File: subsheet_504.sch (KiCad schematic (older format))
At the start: 34 parts, among them J502 Phono LEFT, J503 Phono RIGHT, U504 LF347N_mu, U508 LMC1992CCN_PHY

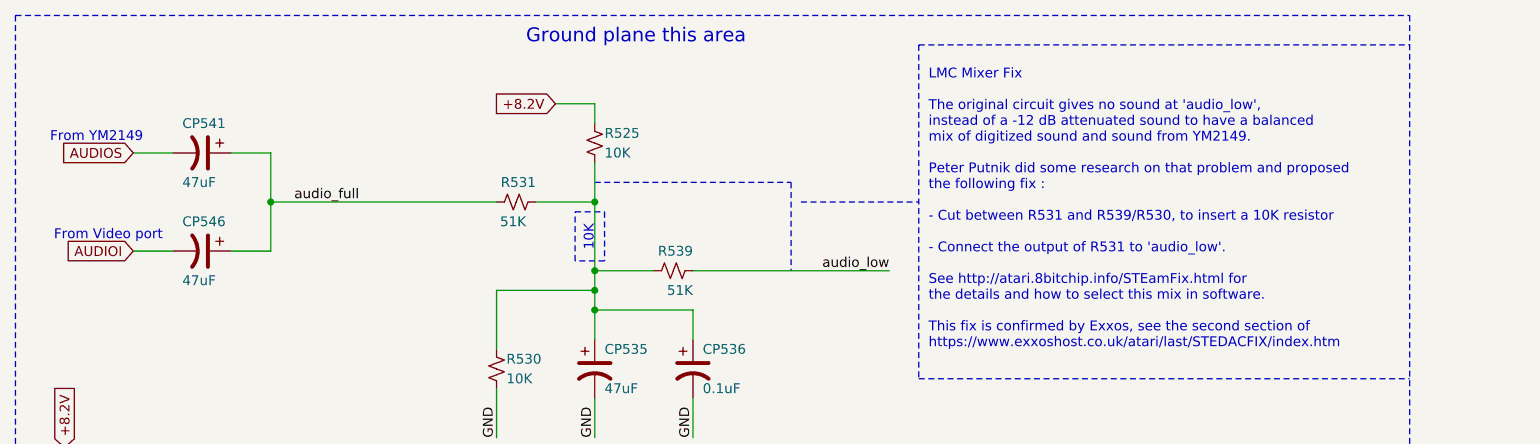
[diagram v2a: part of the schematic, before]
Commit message: Resolves #18 : Apply the LMC mixer fix
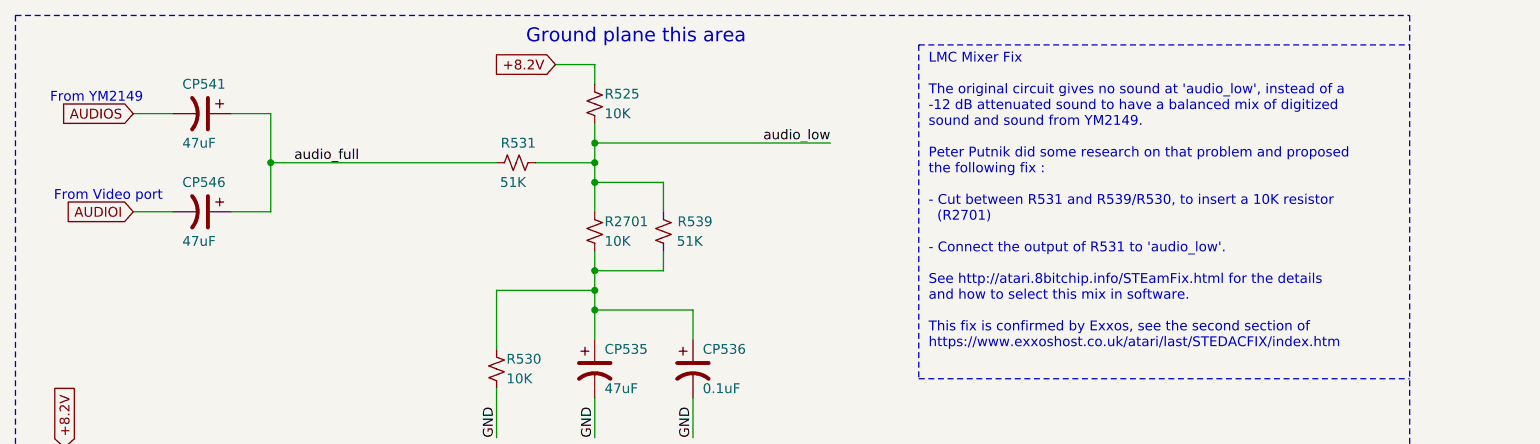
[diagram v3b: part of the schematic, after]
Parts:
- added R2701: 10K, commons_passives_THT:Passive_THT_resistor_W2.54mm_L12.70mm, symbol Device:R_Small_US
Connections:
- net audio_low: now also R525.2, R531.2, R2701.1
- net at CP535.1, CP536.1, R530.1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: now also R2701.2; no longer R525.2, R531.2
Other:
- note added: "LMC Mixer Fix\n\nThe original circuit gives no sound at 'audio_low', instead of a \n-12 dB attenuated sound to have a balanced mix of digitized \nsound and sound from YM2149.\n\nPeter Putnik did some research on that problem and proposed \nthe following fix :\n\n- Cut between R531 and R539/R530, to insert a 10K resistor \n (R2701)\n \n- Connect the output of R531 to 'audio_low'. \n\nSee http://at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"
- note removed: "10K"
- note removed: "LMC Mixer Fix\n\nThe original circuit gives no sound at 'audio_low',\ninstead of a -12 dB attenuated sound to have a balanced\nmix of digitized sound and sound from YM2149.\n\nPeter Putnik did some research on that problem and proposed \nthe following fix :\n\n- Cut between R531 and R539/R530, to insert a 10K resistor\n \n- Connect the output of R531 to 'audio_low'. \n\nSee http://atari.8bitchip.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"
- moved on the sheet: CP541, CP546, R525, R531, R539
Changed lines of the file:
@@
 Text GLabel 1000 3800 0    50   Output ~ 0
 GIL
-Text GLabel 1150 1250 0    50   Input ~ 0
+Text GLabel 1150 1050 0    50   Input ~ 0
 AUDIOS
-Text GLabel 1150 1750 0    50   Input ~ 0
+Text GLabel 1150 1550 0    50   Input ~ 0
 AUDIOI
 NoConn ~ 2900 3600
@@
 L Device:CP1 C?
 U 1 1 60CF0999
-P 1500 1250
+P 1500 1050
 AR Path="/6089D0C2/60CF0999" Ref="C?"  Part="1"
 AR Path="/60B8B7AD/60CF0999" Ref="C?"  Part="1"
@@
 AR Path="/60CC3B10/60CF0999" Ref="C?"  Part="1"
 AR Path="/60CD36E9/60CF0999" Ref="CP541"  Part="1"
-F 0 "CP541" V 1350 1150 50  0000 L CNN
-F 1 "47uF" V 1650 1150 50  0000 L CNN
-F 2 "commons_passives_THT:Passive_THT_capacitor_polarized_W6.35mm_L20.32mm" H 1500 1250 50  0001 C CNN
-F 3 "~" H 1500 1250 50  0001 C CNN
-	1    1500 1250
+F 0 "CP541" V 1350 950 50  0000 L CNN
+F 1 "47uF" V 1650 950 50  0000 L CNN
+F 2 "commons_passives_THT:Passive_THT_capacitor_polarized_W6.35mm_L20.32mm" H 1500 1050 50  0001 C CNN
+F 3 "~" H 1500 1050 50  0001 C CNN
+	1    1500 1050
 	0    1    1    0
 $EndComp
 Wire Wire Line
-	1650 1250 1850 1250
-Wire Wire Line
-	1150 1250 1350 1250
+	1650 1050 1850 1050
+Wire Wire Line
+	1150 1050 1350 1050
 $Comp
 L Device:CP1 C?
 U 1 1 60CF36CC
-P 1500 1750
+P 1500 1550
 AR Path="/6089D0C2/60CF36CC" Ref="C?"  Part="1"
 AR Path="/60B8B7AD/60CF36CC" Ref="C?"  Part="1"
@@
 AR Path="/60CC3B10/60CF36CC" Ref="C?"  Part="1"
 AR Path="/60CD36E9/60CF36CC" Ref="CP546"  Part="1"
-F 0 "CP546" V 1350 1650 50  0000 L CNN
-F 1 "47uF" V 1650 1650 50  0000 L CNN
-F 2 "commons_passives_THT:Passive_THT_capacitor_polarized_W6.35mm_L20.32mm" H 1500 1750 50  0001 C CNN
-F 3 "~" H 1500 1750 50  0001 C CNN
-	1    1500 1750
+F 0 "CP546" V 1350 1450 50  0000 L CNN
+F 1 "47uF" V 1650 1450 50  0000 L CNN
+F 2 "commons_passives_THT:Passive_THT_capacitor_polarized_W6.35mm_L20.32mm" H 1500 1550 50  0001 C CNN
+F 3 "~" H 1500 1550 50  0001 C CNN
+	1    1500 1550
 	0    1    1    0
 $EndComp
 Wire Wire Line
-	1650 1750 1850 1750
-Wire Wire Line
-	1150 1750 1350 1750
+	1650 1550 1850 1550
+Wire Wire Line
+	1150 1550 1350 1550
 $Comp
 L Device:CP1 C?
@@
 L Device:R_Small_US R?
 U 1 1 60CF6F70
-P 3500 1200
+P 3500 1000
 AR Path="/60B3D9E3/60CF6F70" Ref="R?"  Part="1"
 AR Path="/60B8B7AD/60CF6F70" Ref="R?"  Part="1"
@@
 AR Path="/60CC3B10/60CF6F70" Ref="R?"  Part="1"
 AR Path="/60CD36E9/60CF6F70" Ref="R525"  Part="1"
-F 0 "R525" H 3550 1250 50  0000 L CNN
-F 1 "10K" H 3550 1150 50  0000 L CNN
-F 2 "commons_passives_THT:Passive_THT_resistor_W2.54mm_L12.70mm" H 3500 1200 50  0001 C CNN
-F 3 "~" H 3500 1200 50  0001 C CNN
-	1    3500 1200
+F 0 "R525" H 3550 1050 50  0000 L CNN
+F 1 "10K" H 3550 950 50  0000 L CNN
+F 2 "commons_passives_THT:Passive_THT_resistor_W2.54mm_L12.70mm" H 3500 1000 50  0001 C CNN
+F 3 "~" H 3500 1000 50  0001 C CNN
+	1    3500 1000
 	1    0    0    -1
 $EndComp
 Text Label 3000 2700 1    50   ~ 0
 GND
-Text GLabel 3300 1000 0    50   Input ~ 0
+Text GLabel 3300 800  0    50   Input ~ 0
 +8.2V
 Wire Wire Line
@@
 Wire Wire Line
 	3000 2450 3000 2700
-Text Notes 1200 1200 2    50   ~ 0
+Text Notes 1200 1000 2    50   ~ 0
 From YM2149
-Text Notes 1300 1700 2    50   ~ 0
+Text Notes 1300 1500 2    50   ~ 0
 From Video port
-Text Label 2300 1500 2    50   ~ 0
+Text Label 2300 1300 2    50   ~ 0
 audio_full
 $Comp
 L Device:R_Small_US R?
 U 1 1 60D12893
-P 3100 1500
+P 3100 1300
 AR Path="/60B3D9E3/60D12893" Ref="R?"  Part="1"
 AR Path="/60B8B7AD/60D12893" Ref="R?"  Part="1"
@@
 AR Path="/60CC3B10/60D12893" Ref="R?"  Part="1"
 AR Path="/60CD36E9/60D12893" Ref="R531"  Part="1"
-F 0 "R531" V 3200 1400 50  0000 L CNN
-F 1 "51K" V 3000 1450 50  0000 L CNN
-F 2 "commons_passives_THT:Passive_THT_resistor_W2.54mm_L12.70mm" H 3100 1500 50  0001 C CNN
-F 3 "~" H 3100 1500 50  0001 C CNN
-	1    3100 1500
+F 0 "R531" V 3200 1200 50  0000 L CNN
+F 1 "51K" V 3000 1250 50  0000 L CNN
+F 2 "commons_passives_THT:Passive_THT_resistor_W2.54mm_L12.70mm" H 3100 1300 50  0001 C CNN
+F 3 "~" H 3100 1300 50  0001 C CNN
+	1    3100 1300
 	0    -1   -1   0
 $EndComp
@@
 L Device:R_Small_US R?
 U 1 1 60D13044
-P 3900 1850
+P 3850 1650
 AR Path="/60B3D9E3/60D13044" Ref="R?"  Part="1"
 AR Path="/60B8B7AD/60D13044" Ref="R?"  Part="1"
@@
 AR Path="/60CC3B10/60D13044" Ref="R?"  Part="1"
 AR Path="/60CD36E9/60D13044" Ref="R539"  Part="1"
-F 0 "R539" V 4000 1750 50  0000 L CNN
-F 1 "51K" V 3800 1750 50  0000 L CNN
-F 2 "commons_passives_THT:Passive_THT_resistor_W2.54mm_L12.70mm" H 3900 1850 50  0001 C CNN
-F 3 "~" H 3900 1850 50  0001 C CNN
-	1    3900 1850
-	0    -1   -1   0
-$EndComp
-Text Label 5000 1850 2    50   ~ 0
+F 0 "R539" H 3600 1600 50  0000 L CNN
+F 1 "51K" H 3650 1700 50  0000 L CNN
+F 2 "commons_passives_THT:Passive_THT_resistor_W2.54mm_L12.70mm" H 3850 1650 50  0001 C CNN
+F 3 "~" H 3850 1650 50  0001 C CNN
+	1    3850 1650
+	-1   0    0    1
+$EndComp
+Text Label 4700 1200 2    50   ~ 0
 audio_low
 $Comp
@@
 	2450 3300 2900 3300
 Wire Wire Line
-	3200 1500 3500 1500
-Wire Wire Line
-	3300 1000 3500 1000
+	3200 1300 3500 1300
+Wire Wire Line
+	3300 800  3500 800
 Wire Wire Line
 	1550 4000 1650 4000
@@
 	1650 3900 2900 3900
 Wire Wire Line
-	1850 1250 1850 1500
-Wire Wire Line
-	3500 1850 3800 1850
-Wire Wire Line
-	1850 1500 3000 1500
-Connection ~ 1850 1500
-Wire Wire Line
-	1850 1500 1850 1750
+	1850 1050 1850 1300
+Wire Wire Line
+	1850 1300 3000 1300
+Connection ~ 1850 1300
+Wire Wire Line
+	1850 1300 1850 1550
 Wire Wire Line
 	3000 1950 3500 1950
@@
 Wire Wire Line
 	3000 1950 3000 2250
-Connection ~ 3500 1500
-Wire Wire Line
-	4000 1850 5000 1850
 Wire Wire Line
 	1550 3800 2900 3800
@@
 	7450 4200 7450 4850
 Text Notes 5200 2250 0    50   ~ 0
-LMC Mixer Fix\n\nThe original circuit gives no sound at 'audio_low',\ninstead of a -12 dB attenuated sound to have a balanced\nmix of digitized sound and sound from YM2149.\n\nPeter Putnik did some research on that problem and proposed \nthe following fix :\n\n- Cut between R531 and R539/R530, to insert a 10K resistor\n  \n- Connect the output of R531 to 'audio_low'. \n\nSee http://atari.8bitchip.info/STEamFix.html for \nthe details and how to select this mix in software.\n\nThis fix is confirmed by Exxos, see the second section of\nhttps://www.exxoshost.co.uk/atari/last/STEDACFIX/index.htm\n
+LMC Mixer Fix\n\nThe original circuit gives no sound at 'audio_low', instead of a \n-12 dB attenuated sound to have a balanced mix of digitized \nsound and sound from YM2149.\n\nPeter Putnik did some research on that problem and proposed \nthe following fix :\n\n- Cut between R531 and R539/R530, to insert a 10K resistor \n  (R2701)\n  \n- Connect the output of R531 to 'audio_low'. \n\nSee http://atari.8bitchip.info/STEamFix.html for the details \nand how to select this mix in software.\n\nThis fix is confirmed by Exxos, see the second section of\nhttps://www.exxoshost.co.uk/atari/last/STEDACFIX/index.htm\n
 Connection ~ 3500 1950
-Text Notes 3500 1750 1    50   ~ 0
-10K
-Wire Notes Line
-	3400 1550 3550 1550
-Wire Notes Line
-	3550 1550 3550 1800
-Wire Notes Line
-	3550 1800 3400 1800
-Wire Notes Line
-	3400 1800 3400 1550
-Wire Wire Line
-	3500 1100 3500 1000
-Wire Wire Line
-	3500 1300 3500 1500
-Wire Notes Line
-	3500 1400 4500 1400
-Connection ~ 3500 1850
+Wire Wire Line
+	3500 900  3500 800
 Wire Wire Line
 	3500 1850 3500 1950
-Wire Wire Line
-	3500 1500 3500 1850
-Wire Notes Line
-	4500 1400 4500 1850
 Wire Notes Line
 	5150 700  5150 2400
-Wire Notes Line
-	4550 1500 5150 1500
 Wire Notes Line
 	5150 700  7650 700
@@
 Wire Wire Line
 	1000 3800 1250 3800
+$Comp
+L Device:R_Small_US R?
+U 1 1 620C294B
+P 3500 1650
+AR Path="/60B3D9E3/620C294B" Ref="R?"  Part="1"
+AR Path="/60B8B7AD/620C294B" Ref="R?"  Part="1"
+AR Path="/60C95DE8/620C294B" Ref="R?"  Part="1"
+AR Path="/60CC3B10/620C294B" Ref="R?"  Part="1"
+AR Path="/60CD36E9/620C294B" Ref="R2701"  Part="1"
+F 0 "R2701" H 3550 1700 50  0000 L CNN
+F 1 "10K" H 3550 1600 50  0000 L CNN
+F 2 "commons_passives_THT:Passive_THT_resistor_W2.54mm_L12.70mm" H 3500 1650 50  0001 C CNN
+F 3 "~" H 3500 1650 50  0001 C CNN
+	1    3500 1650
+	1    0    0    -1
+$EndComp
+Connection ~ 3500 1300
+Wire Wire Line
+	3500 1300 3500 1400
+Wire Wire Line
+	3500 1750 3500 1850
+Connection ~ 3500 1850
+Wire Wire Line
+	3500 1400 3850 1400
+Connection ~ 3500 1400
+Wire Wire Line
+	3500 1400 3500 1550
+Wire Wire Line
+	3850 1850 3850 1750
+Wire Wire Line
+	3500 1850 3850 1850
+Wire Wire Line
+	3850 1550 3850 1400
+Wire Wire Line
+	3500 1100 3500 1200
+Wire Wire Line
+	3500 1200 4700 1200
+Connection ~ 3500 1200
+Wire Wire Line
+	3500 1200 3500 1300
 $EndSCHEMATC

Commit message: Resolves #13 : assign 1206 hand-solder footprints to resistors
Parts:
- R2701, R520, R524, R525, R527, R530, R531, R533, R537, R538, R539, R540, R541, R590, R591: footprint commons_passives_THT:Passive_THT_resistor_W2.54mm_L12.70mm -> Resistor_SMD:R_1206_3216Metric_Pad1.30x1.75mm_HandSolder
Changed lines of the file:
@@
 F 0 "R530" H 3050 2400 50  0000 L CNN
 F 1 "10K" H 3050 2300 50  0000 L CNN
-F 2 "commons_passives_THT:Passive_THT_resistor_W2.54mm_L12.70mm" H 3000 2350 50  0001 C CNN
+F 2 "Resistor_SMD:R_1206_3216Metric_Pad1.30x1.75mm_HandSolder" H 3000 2350 50  0001 C CNN
 F 3 "~" H 3000 2350 50  0001 C CNN
 	1    3000 2350
@@
 F 0 "R525" H 3550 1050 50  0000 L CNN
 F 1 "10K" H 3550 950 50  0000 L CNN
-F 2 "commons_passives_THT:Passive_THT_resistor_W2.54mm_L12.70mm" H 3500 1000 50  0001 C CNN
+F 2 "Resistor_SMD:R_1206_3216Metric_Pad1.30x1.75mm_HandSolder" H 3500 1000 50  0001 C CNN
 F 3 "~" H 3500 1000 50  0001 C CNN
 	1    3500 1000
@@
 F 0 "R531" V 3200 1200 50  0000 L CNN
 F 1 "51K" V 3000 1250 50  0000 L CNN
-F 2 "commons_passives_THT:Passive_THT_resistor_W2.54mm_L12.70mm" H 3100 1300 50  0001 C CNN
+F 2 "Resistor_SMD:R_1206_3216Metric_Pad1.30x1.75mm_HandSolder" H 3100 1300 50  0001 C CNN
 F 3 "~" H 3100 1300 50  0001 C CNN
 	1    3100 1300
@@
 F 0 "R539" H 3600 1600 50  0000 L CNN
 F 1 "51K" H 3650 1700 50  0000 L CNN
-F 2 "commons_passives_THT:Passive_THT_resistor_W2.54mm_L12.70mm" H 3850 1650 50  0001 C CNN
+F 2 "Resistor_SMD:R_1206_3216Metric_Pad1.30x1.75mm_HandSolder" H 3850 1650 50  0001 C CNN
 F 3 "~" H 3850 1650 50  0001 C CNN
 	1    3850 1650
@@
 F 0 "R520" H 1900 5450 50  0000 C CNN
 F 1 "1K" H 1900 5550 50  0000 C CNN
-F 2 "commons_passives_THT:Passive_THT_resistor_W2.54mm_L12.70mm" H 1750 5500 50  0001 C CNN
+F 2 "Resistor_SMD:R_1206_3216Metric_Pad1.30x1.75mm_HandSolder" H 1750 5500 50  0001 C CNN
 F 3 "~" H 1750 5500 50  0001 C CNN
 	1    1750 5500
@@
 F 0 "R590" V 1400 7400 50  0000 L CNN
 F 1 "270K" V 1600 7400 50  0000 L CNN
-F 2 "commons_passives_THT:Passive_THT_resistor_W2.54mm_L12.70mm" H 1500 7500 50  0001 C CNN
+F 2 "Resistor_SMD:R_1206_3216Metric_Pad1.30x1.75mm_HandSolder" H 1500 7500 50  0001 C CNN
 F 3 "~" H 1500 7500 50  0001 C CNN
 	1    1500 7500
@@
 F 0 "R533" H 6350 5450 50  0000 C CNN
 F 1 "1K" H 6350 5550 50  0000 C CNN
-F 2 "commons_passives_THT:Passive_THT_resistor_W2.54mm_L12.70mm" H 6500 5500 50  0001 C CNN
+F 2 "Resistor_SMD:R_1206_3216Metric_Pad1.30x1.75mm_HandSolder" H 6500 5500 50  0001 C CNN
 F 3 "~" H 6500 5500 50  0001 C CNN
 	1    6500 5500
@@
 F 0 "R591" V 6150 7400 50  0000 L CNN
 F 1 "270K" V 6350 7400 50  0000 L CNN
-F 2 "commons_passives_THT:Passive_THT_resistor_W2.54mm_L12.70mm" H 6250 7500 50  0001 C CNN
+F 2 "Resistor_SMD:R_1206_3216Metric_Pad1.30x1.75mm_HandSolder" H 6250 7500 50  0001 C CNN
 F 3 "~" H 6250 7500 50  0001 C CNN
 	1    6250 7500
@@
 F 0 "R527" H 2100 5700 50  0000 C CNN
 F 1 "10K" H 2100 5800 50  0000 C CNN
-F 2 "commons_passives_THT:Passive_THT_resistor_W2.54mm_L12.70mm" H 2250 5750 50  0001 C CNN
+F 2 "Resistor_SMD:R_1206_3216Metric_Pad1.30x1.75mm_HandSolder" H 2250 5750 50  0001 C CNN
 F 3 "~" H 2250 5750 50  0001 C CNN
 	1    2250 5750
@@
 F 0 "R524" V 2850 5750 50  0000 L CNN
 F 1 "3K6" V 2850 6150 50  0000 L CNN
-F 2 "commons_passives_THT:Passive_THT_resistor_W2.54mm_L12.70mm" H 2900 6050 50  0001 C CNN
+F 2 "Resistor_SMD:R_1206_3216Metric_Pad1.30x1.75mm_HandSolder" H 2900 6050 50  0001 C CNN
 F 3 "~" H 2900 6050 50  0001 C CNN
 	1    2900 6050
@@
 F 0 "R540" H 3400 6700 50  0000 C CNN
 F 1 "1K" H 3400 6800 50  0000 C CNN
-F 2 "commons_passives_THT:Passive_THT_resistor_W2.54mm_L12.70mm" H 3550 6750 50  0001 C CNN
+F 2 "Resistor_SMD:R_1206_3216Metric_Pad1.30x1.75mm_HandSolder" H 3550 6750 50  0001 C CNN
 F 3 "~" H 3550 6750 50  0001 C CNN
 	1    3550 6750
@@
 F 0 "R538" H 5850 5700 50  0000 C CNN
 F 1 "10K" H 5850 5800 50  0000 C CNN
-F 2 "commons_passives_THT:Passive_THT_resistor_W2.54mm_L12.70mm" H 6000 5750 50  0001 C CNN
+F 2 "Resistor_SMD:R_1206_3216Metric_Pad1.30x1.75mm_HandSolder" H 6000 5750 50  0001 C CNN
 F 3 "~" H 6000 5750 50  0001 C CNN
 	1    6000 5750
@@
 F 0 "R537" V 5400 6150 50  0000 L CNN
 F 1 "3K6" V 5400 5800 50  0000 L CNN
-F 2 "commons_passives_THT:Passive_THT_resistor_W2.54mm_L12.70mm" H 5350 6050 50  0001 C CNN
+F 2 "Resistor_SMD:R_1206_3216Metric_Pad1.30x1.75mm_HandSolder" H 5350 6050 50  0001 C CNN
 F 3 "~" H 5350 6050 50  0001 C CNN
 	1    5350 6050
@@
 F 0 "R541" H 4550 6700 50  0000 C CNN
 F 1 "1K" H 4550 6800 50  0000 C CNN
-F 2 "commons_passives_THT:Passive_THT_resistor_W2.54mm_L12.70mm" H 4700 6750 50  0001 C CNN
+F 2 "Resistor_SMD:R_1206_3216Metric_Pad1.30x1.75mm_HandSolder" H 4700 6750 50  0001 C CNN
 F 3 "~" H 4700 6750 50  0001 C CNN
 	1    4700 6750
@@
 F 0 "R2701" H 3550 1700 50  0000 L CNN
 F 1 "10K" H 3550 1600 50  0000 L CNN
-F 2 "commons_passives_THT:Passive_THT_resistor_W2.54mm_L12.70mm" H 3500 1650 50  0001 C CNN
+F 2 "Resistor_SMD:R_1206_3216Metric_Pad1.30x1.75mm_HandSolder" H 3500 1650 50  0001 C CNN
 F 3 "~" H 3500 1650 50  0001 C CNN
 	1    3500 1650

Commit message: Resolves #8 : Assign 1206 hand-solder footprints to non polarized capacitors
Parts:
- C524: footprint commons_passives_THT:Passive_THT_capacitor_mlcc_W2.54mm_L7.62mm -> Capacitor_SMD:C_1206_3216Metric_Pad1.33x1.80mm_HandSolder
- C528, C531, C534, C538: footprint commons_passives_THT:Passive_THT_capacitor_mlcc_W2.54mm_L10.16mm -> Capacitor_SMD:C_1206_3216Metric_Pad1.33x1.80mm_HandSolder
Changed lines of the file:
@@
 F 0 "C528" V 1950 4050 50  0000 L CNN
 F 1 "0.0082uF" V 1850 3950 50  0000 L CNN
-F 2 "commons_passives_THT:Passive_THT_capacitor_mlcc_W2.54mm_L10.16mm" H 2038 3850 50  0001 C CNN
+F 2 "Capacitor_SMD:C_1206_3216Metric_Pad1.33x1.80mm_HandSolder" H 2038 3850 50  0001 C CNN
 F 3 "~" H 2000 4000 50  0001 C CNN
 	1    2000 4000
@@
 F 0 "C531" H 500 4950 50  0000 L CNN
 F 1 "0.0082uF" H 350 5050 50  0000 L CNN
-F 2 "commons_passives_THT:Passive_THT_capacitor_mlcc_W2.54mm_L10.16mm" H 838 4850 50  0001 C CNN
+F 2 "Capacitor_SMD:C_1206_3216Metric_Pad1.33x1.80mm_HandSolder" H 838 4850 50  0001 C CNN
 F 3 "~" H 800 5000 50  0001 C CNN
 	1    800  5000
@@
 F 0 "C534" H 7600 4950 50  0000 L CNN
 F 1 "0.0082uF" H 7550 5050 50  0000 L CNN
-F 2 "commons_passives_THT:Passive_THT_capacitor_mlcc_W2.54mm_L10.16mm" H 7488 4850 50  0001 C CNN
+F 2 "Capacitor_SMD:C_1206_3216Metric_Pad1.33x1.80mm_HandSolder" H 7488 4850 50  0001 C CNN
 F 3 "~" H 7450 5000 50  0001 C CNN
 	1    7450 5000
@@
 F 0 "C538" V 6300 3950 50  0000 L CNN
 F 1 "0.0082uF" V 6400 3900 50  0000 L CNN
-F 2 "commons_passives_THT:Passive_THT_capacitor_mlcc_W2.54mm_L10.16mm" H 6288 3750 50  0001 C CNN
+F 2 "Capacitor_SMD:C_1206_3216Metric_Pad1.33x1.80mm_HandSolder" H 6288 3750 50  0001 C CNN
 F 3 "~" H 6250 3900 50  0001 C CNN
 	1    6250 3900
@@
 F 0 "C524" H 825 3100 50  0000 L CNN
 F 1 "0.1uF" H 825 2900 50  0000 L CNN
-F 2 "commons_passives_THT:Passive_THT_capacitor_mlcc_W2.54mm_L7.62mm" H 838 2850 50  0001 C CNN
+F 2 "Capacitor_SMD:C_1206_3216Metric_Pad1.33x1.80mm_HandSolder" H 838 2850 50  0001 C CNN
 F 3 "~" H 800 3000 50  0001 C CNN
 	1    800  3000

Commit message: Resolves #20 : Replace polarized capacitors CP101 and CP536 by unpolarized ones
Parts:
- C536: renamed from CP536; footprint commons_passives_THT:Passive_THT_capacitor_mlcc_W2.54mm_L7.62mm -> Capacitor_SMD:C_1206_3216Metric_Pad1.33x1.80mm_HandSolder; symbol Device:CP1 -> Device:C_Small
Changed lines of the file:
@@
 $EndComp
 $Comp
-L Device:CP1 C?
+L Device:C_Small C?
 U 1 1 60CEE43A
 P 4000 2350
@@
 AR Path="/60C95DE8/60CEE43A" Ref="C?"  Part="1"
 AR Path="/60CC3B10/60CEE43A" Ref="C?"  Part="1"
-AR Path="/60CD36E9/60CEE43A" Ref="CP536"  Part="1"
-F 0 "CP536" H 4050 2450 50  0000 L CNN
+AR Path="/60CD36E9/60CEE43A" Ref="C536"  Part="1"
+F 0 "C536" H 4050 2450 50  0000 L CNN
 F 1 "0.1uF" H 4050 2250 50  0000 L CNN
-F 2 "commons_passives_THT:Passive_THT_capacitor_mlcc_W2.54mm_L7.62mm" H 4000 2350 50  0001 C CNN
+F 2 "Capacitor_SMD:C_1206_3216Metric_Pad1.33x1.80mm_HandSolder" H 4000 2350 50  0001 C CNN
 F 3 "~" H 4000 2350 50  0001 C CNN
 	1    4000 2350
@@
 Text Label 3500 2700 1    50   ~ 0
 GND
-Wire Wire Line
-	4000 2700 4000 2500
 Text Label 4000 2700 1    50   ~ 0
 GND
@@
 Text GLabel 3300 800  0    50   Input ~ 0
 +8.2V
-Wire Wire Line
-	4000 2050 4000 2200
 Wire Wire Line
 	3000 2450 3000 2700
@@
 Wire Wire Line
 	3500 1200 3500 1300
+Wire Wire Line
+	4000 2050 4000 2250
+Wire Wire Line
+	4000 2450 4000 2700
 $EndSCHEMATC
